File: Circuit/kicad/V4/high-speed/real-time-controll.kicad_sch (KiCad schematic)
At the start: 32 parts, among them J6 RGB-BTN, U12 ESP32-S3-WROOM-1, U19 MCP23S17_SS, U20 CD74HC154M

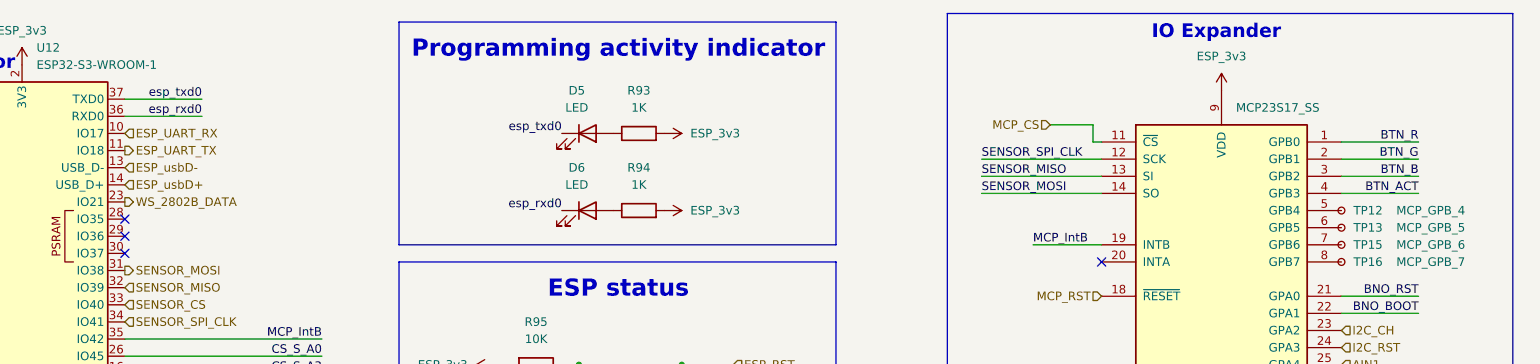
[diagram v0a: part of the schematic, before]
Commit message: High Speed all routed, DRC, DFM shows 0 error (without silkscreen layers)
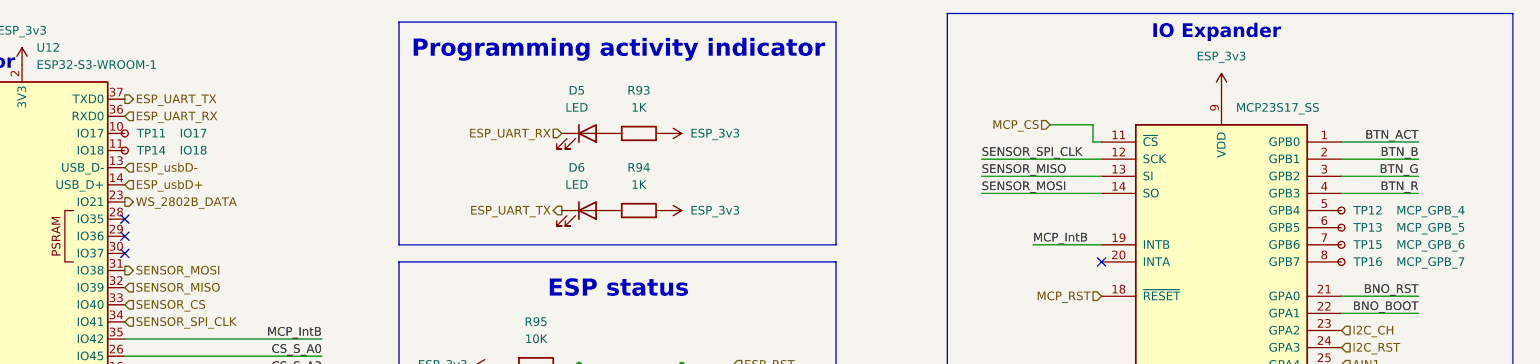
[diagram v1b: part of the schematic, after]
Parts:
- added TP11: IO17, TestPoint:TestPoint_Pad_D2.0mm, symbol Connector:TestPoint_Small
- added TP14: IO18, TestPoint:TestPoint_Pad_D2.0mm, symbol Connector:TestPoint_Small
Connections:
- net BTN_ACT: now also U19.1 (GPB0); no longer U19.4 (GPB3)
- net BTN_B: now also U19.2 (GPB1); no longer U19.3 (GPB2)
- net BTN_G: now also U19.3 (GPB2); no longer U19.2 (GPB1)
- net BTN_R: now also U19.4 (GPB3); no longer U19.1 (GPB0)
- net ESP_UART_RX: now also D5.1 (K), U12.36 (RXD0); no longer U12.10 (IO17)
- net ESP_UART_TX: now also D6.1 (K), U12.37 (TXD0); no longer U12.11 (IO18)
- removed net esp_rxd0: D6.1 (K), U12.36 (RXD0)
- removed net esp_txd0: D5.1 (K), U12.37 (TXD0)
- new net: TP11.1, U12.10 (IO17)
- new net: TP14.1, U12.11 (IO18)
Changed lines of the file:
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@@
 	(wire
 		(pts
-			(xy 260.35 39.37) (xy 248.92 39.37)
+			(xy 260.35 31.75) (xy 248.92 31.75)
 		)
 		(stroke
@@
 	(wire
 		(pts
-			(xy 260.35 31.75) (xy 248.92 31.75)
+			(xy 260.35 39.37) (xy 248.92 39.37)
 		)
 		(stroke
@@
 	(wire
 		(pts
-			(xy 68.58 27.94) (xy 80.01 27.94)
-		)
-		(stroke
-			(width 0)
-			(type default)
-		)
-	)
-	(wire
-		(pts
 			(xy 208.28 68.58) (xy 213.36 68.58)
 		)
@@
 	(wire
 		(pts
-			(xy 260.35 36.83) (xy 248.92 36.83)
+			(xy 260.35 34.29) (xy 248.92 34.29)
 		)
 		(stroke
@@
 	(wire
 		(pts
-			(xy 260.35 34.29) (xy 248.92 34.29)
+			(xy 260.35 36.83) (xy 248.92 36.83)
 		)
 		(stroke
@@
 	(wire
 		(pts
-			(xy 68.58 25.4) (xy 80.01 25.4)
-		)
-		(stroke
-			(width 0)
-			(type default)
-		)
-	)
-	(wire
-		(pts
 			(xy 77.47 125.73) (xy 95.25 125.73)
 		)
@@
 		)
 	)
-	(label "esp_rxd0"
-		(at 133.35 41.91 180)
-		(effects
-			(font
-				(size 1.27 1.27)
-			)
-			(justify right bottom)
-		)
-	)
 	(label "SENSOR_MOSI"
 		(at 77.47 143.51 0)
@@
 	)
 	(label "BTN_G"
-		(at 260.35 34.29 180)
+		(at 260.35 36.83 180)
 		(effects
 			(font
@@
 	)
 	(label "BTN_R"
-		(at 260.35 31.75 180)
+		(at 260.35 39.37 180)
 		(effects
 			(font
@@
 	)
 	(label "BTN_ACT"
-		(at 260.35 39.37 180)
+		(at 260.35 31.75 180)
 		(effects
 			(font
@@
 		)
 	)
-	(label "esp_rxd0"
-		(at 80.01 27.94 180)
-		(effects
-			(font
-				(size 1.27 1.27)
-			)
-			(justify right bottom)
-		)
-	)
 	(label "SPI_DIAG0"
 		(at 210.82 142.24 180)
@@
 		)
 	)
-	(label "esp_txd0"
-		(at 80.01 25.4 180)
-		(effects
-			(font
-				(size 1.27 1.27)
-			)
-			(justify right bottom)
-		)
-	)
 	(label "SENSOR_MISO"
 		(at 27.94 114.3 0)
@@
 	)
 	(label "BTN_B"
-		(at 260.35 36.83 180)
+		(at 260.35 34.29 180)
 		(effects
 			(font
@@
 		)
 	)
-	(label "esp_txd0"
-		(at 133.35 30.48 180)
-		(effects
-			(font
-				(size 1.27 1.27)
-			)
-			(justify right bottom)
-		)
-	)
 	(label "BTN_R"
 		(at 243.84 95.25 0)
@@
 		)
 	)
+	(hierarchical_label "ESP_UART_RX"
+		(shape input)
+		(at 68.58 27.94 0)
+		(effects
+			(font
+				(size 1.27 1.27)
+			)
+			(justify left)
+		)
+	)
 	(hierarchical_label "MCP_CS"
 		(shape input)
@@
 		)
 	)
+	(hierarchical_label "ESP_UART_TX"
+		(shape output)
+		(at 68.58 25.4 0)
+		(effects
+			(font
+				(size 1.27 1.27)
+			)
+			(justify left)
+		)
+	)
 	(hierarchical_label "I2C_RST"
 		(shape input)
@@
 		)
 	)
+	(hierarchical_label "ESP_UART_TX"
+		(shape output)
+		(at 133.35 41.91 180)
+		(effects
+			(font
+				(size 1.27 1.27)
+			)
+			(justify right)
+		)
+	)
 	(hierarchical_label "ESP_usbD+"
 		(shape input)
@@
 		)
 	)
+	(hierarchical_label "ESP_UART_RX"
+		(shape input)
+		(at 133.35 30.48 180)
+		(effects
+			(font
+				(size 1.27 1.27)
+			)
+			(justify right)
+		)
+	)
 	(hierarchical_label "RPI_MOSI"
 		(shape output)
@@
 		)
 	)
-	(hierarchical_label "ESP_UART_RX"
-		(shape input)
-		(at 68.58 30.48 0)
-		(effects
-			(font
-				(size 1.27 1.27)
-			)
-			(justify left)
-		)
-	)
-	(hierarchical_label "ESP_UART_TX"
-		(shape output)
-		(at 68.58 33.02 0)
-		(effects
-			(font
-				(size 1.27 1.27)
-			)
-			(justify left)
-		)
-	)
 	(hierarchical_label "MCP_RST"
 		(shape input)
@@
 	)
 	(symbol
+		(lib_id "Connector:TestPoint_Small")
+		(at 68.58 30.48 0)
+		(unit 1)
+		(exclude_from_sim no)
+		(in_bom no)
+		(on_board yes)
+		(dnp no)
+		(property "Reference" "TP11"
+			(at 70.358 30.48 0)
+			(effects
+				(font
+					(size 1.27 1.27)
+				)
+				(justify left)
+			)
+		)
+		(property "Value" "IO17"
+			(at 76.708 30.48 0)
+			(effects
+				(font
+					(size 1.27 1.27)
+				)
+				(justify left)
+			)
+		)
+		(property "Footprint" "TestPoint:TestPoint_Pad_D2.0mm"
+			(at 73.66 30.48 0)
+			(effects
+				(font
+					(size 1.27 1.27)
+				)
+				(hide yes)
+			)
+		)
+		(property "Datasheet" "~"
+			(at 73.66 30.48 0)
+			(effects
+				(font
+					(size 1.27 1.27)
+				)
+				(hide yes)
+			)
+		)
+		(property "Description" "test point"
+			(at 68.58 30.48 0)
+			(effects
+				(font
+					(size 1.27 1.27)
+				)
+				(hide yes)
+			)
+		)
+		(property "Cikkszám" "-"
+			(at 68.58 30.48 0)
+			(effects
+				(font
+					(size 1.27 1.27)
+				)
+				(hide yes)
+			)
+		)
+		(property "Link" "-"
+			(at 68.58 30.48 0)
+			(effects
+				(font
+					(size 1.27 1.27)
+				)
+				(hide yes)
+			)
+		)
+		(pin "1"
+		)
+		(instances
+			(project "high-speed"
+				(path "/e63e39d7-6ac0-4ffd-8aa3-1841a4541b55/e6a127e0-e8a4-4ccd-bbc7-ce5df0e2aadb"
+					(reference "TP11")
+					(unit 1)
+				)
+			)
+		)
+	)
+	(symbol
 		(lib_id "Device:R")
 		(at 129.54 64.77 270)
@@
 					(unit 1)
 				)
+			)
+		)
+	)
+	(symbol
+		(lib_id "Connector:TestPoint_Small")
+		(at 68.58 33.02 0)
+		(unit 1)
+		(exclude_from_sim no)
+		(in_bom no)
+		(on_board yes)
+		(dnp no)
+		(property "Reference" "TP14"
+			(at 70.358 33.02 0)
+			(effects
+				(font
+					(size 1.27 1.27)
+				)
+				(justify left)
+			)
+		)
+		(property "Value" "IO18"
+			(at 76.708 33.02 0)
+			(effects
+				(font
+					(size 1.27 1.27)
+				)
+				(justify left)
+			)
+		)
+		(property "Footprint" "TestPoint:TestPoint_Pad_D2.0mm"
+			(at 73.66 33.02 0)
+			(effects
+				(font
+					(size 1.27 1.27)
+				)
+				(hide yes)
+			)
+		)
+		(property "Datasheet" "~"
+			(at 73.66 33.02 0)
+			(effects
+				(font
+					(size 1.27 1.27)
+				)
+				(hide yes)
+			)
+		)
+		(property "Description" "test point"
+			(at 68.58 33.02 0)
+			(effects
+				(font
+					(size 1.27 1.27)
+				)
+				(hide yes)
+			)
+		)
+		(property "Cikkszám" "-"
+			(at 68.58 33.02 0)
+			(effects
+				(font
+					(size 1.27 1.27)
+				)
+				(hide yes)
+			)
+		)
+		(property "Link" "-"
+			(at 68.58 33.02 0)
+			(effects
+				(font
+					(size 1.27 1.27)
+				)
+				(hide yes)
+			)
+		)
+		(pin "1"
+		)
+		(instances
+			(project "high-speed"
+				(path "/e63e39d7-6ac0-4ffd-8aa3-1841a4541b55/e6a127e0-e8a4-4ccd-bbc7-ce5df0e2aadb"
+					(reference "TP14")
+					(unit 1)
+				)
